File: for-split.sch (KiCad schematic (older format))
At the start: 77 parts, among them J1 TRRS, J2 TRRS, U1 ProMicro

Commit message: Increase size of switch cutouts
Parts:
- MX0:0, MX0:5: footprint idle-hands:MX_CUTOUT_VERT_PAD1 -> idle-hands:MX_CUTOUT_PAD1
- MX0:1, MX0:4: footprint idle-hands:MX_CUTOUT_VERT_PAD3 -> idle-hands:MX_CUTOUT_PAD3
- MX0:2, MX0:3, MX1:0, MX1:1, MX1:2, MX1:3, MX1:4, MX1:5, MX2:0, MX2:1, MX2:2, MX2:3, MX2:4, MX2:5, MX3:0, MX3:1, MX3:2, MX3:3, MX3:4, MX3:5, MX4:2, MX4:3: footprint idle-hands:MX_CUTOUT_VERT -> idle-hands:MX_CUTOUT
- MX4:1, MX4:4: footprint idle-hands:MX2U_CUTOUT_VERT -> idle-hands:MX2U_CUTOUT
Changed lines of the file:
@@
 Sheet 1 1
 Title "For Split - 6x4x2 key split keyboard"
-Date ""
-Rev ""
+Date "2018-03-18"
+Rev "2"
 Comp ""
 Comment1 ""
@@
 F 0 "MX1:0" H 5140 2590 50  0000 C CNN
 F 1 "MX1:11" H 4990 2400 50  0000 C CNN
-F 2 "idle-hands:MX_CUTOUT_VERT" H 4990 2480 60  0001 C CNN
+F 2 "idle-hands:MX_CUTOUT" H 4990 2480 60  0001 C CNN
 F 3 "" H 4990 2480 60  0000 C CNN
 	1    4990 2480
@@
 F 0 "MX1:1" H 6040 2590 50  0000 C CNN
 F 1 "MX1:10" H 5890 2400 50  0000 C CNN
-F 2 "idle-hands:MX_CUTOUT_VERT" H 5890 2480 60  0001 C CNN
+F 2 "idle-hands:MX_CUTOUT" H 5890 2480 60  0001 C CNN
 F 3 "" H 5890 2480 60  0000 C CNN
 	1    5890 2480
@@
 F 0 "MX1:2" H 6940 2590 50  0000 C CNN
 F 1 "MX1:9" H 6790 2400 50  0000 C CNN
-F 2 "idle-hands:MX_CUTOUT_VERT" H 6790 2480 60  0001 C CNN
+F 2 "idle-hands:MX_CUTOUT" H 6790 2480 60  0001 C CNN
 F 3 "" H 6790 2480 60  0000 C CNN
 	1    6790 2480
@@
 F 0 "MX1:3" H 7890 2590 50  0000 C CNN
 F 1 "MX1:8" H 7740 2400 50  0000 C CNN
-F 2 "idle-hands:MX_CUTOUT_VERT" H 7740 2480 60  0001 C CNN
+F 2 "idle-hands:MX_CUTOUT" H 7740 2480 60  0001 C CNN
 F 3 "" H 7740 2480 60  0000 C CNN
 	1    7740 2480
@@
 F 0 "MX1:4" H 8840 2590 50  0000 C CNN
 F 1 "MX1:7" H 8690 2400 50  0000 C CNN
-F 2 "idle-hands:MX_CUTOUT_VERT" H 8690 2480 60  0001 C CNN
+F 2 "idle-hands:MX_CUTOUT" H 8690 2480 60  0001 C CNN
 F 3 "" H 8690 2480 60  0000 C CNN
 	1    8690 2480
@@
 F 0 "MX0:0" H 5140 1840 50  0000 C CNN
 F 1 "MX0:11" H 4990 1650 50  0000 C CNN
-F 2 "idle-hands:MX_CUTOUT_VERT_PAD1" H 4990 1730 60  0001 C CNN
+F 2 "idle-hands:MX_CUTOUT_PAD1" H 4990 1730 60  0001 C CNN
 F 3 "" H 4990 1730 60  0000 C CNN
 	1    4990 1730
@@
 F 0 "MX0:1" H 6040 1840 50  0000 C CNN
 F 1 "MX0:10" H 5890 1650 50  0000 C CNN
-F 2 "idle-hands:MX_CUTOUT_VERT_PAD3" H 5890 1730 60  0001 C CNN
+F 2 "idle-hands:MX_CUTOUT_PAD3" H 5890 1730 60  0001 C CNN
 F 3 "" H 5890 1730 60  0000 C CNN
 	1    5890 1730
@@
 F 0 "MX0:2" H 6940 1840 50  0000 C CNN
 F 1 "MX0:9" H 6790 1650 50  0000 C CNN
-F 2 "idle-hands:MX_CUTOUT_VERT" H 6790 1730 60  0001 C CNN
+F 2 "idle-hands:MX_CUTOUT" H 6790 1730 60  0001 C CNN
 F 3 "" H 6790 1730 60  0000 C CNN
 	1    6790 1730
@@
 F 0 "MX0:3" H 7890 1840 50  0000 C CNN
 F 1 "MX0:8" H 7740 1650 50  0000 C CNN
-F 2 "idle-hands:MX_CUTOUT_VERT" H 7740 1730 60  0001 C CNN
+F 2 "idle-hands:MX_CUTOUT" H 7740 1730 60  0001 C CNN
 F 3 "" H 7740 1730 60  0000 C CNN
 	1    7740 1730
@@
 F 0 "MX0:4" H 8840 1840 50  0000 C CNN
 F 1 "MX0:7" H 8690 1650 50  0000 C CNN
-F 2 "idle-hands:MX_CUTOUT_VERT_PAD3" H 8690 1730 60  0001 C CNN
+F 2 "idle-hands:MX_CUTOUT_PAD3" H 8690 1730 60  0001 C CNN
 F 3 "" H 8690 1730 60  0000 C CNN
 	1    8690 1730
@@
 F 0 "MX2:0" H 5140 3340 50  0000 C CNN
 F 1 "MX2:11" H 4990 3150 50  0000 C CNN
-F 2 "idle-hands:MX_CUTOUT_VERT" H 4990 3230 60  0001 C CNN
+F 2 "idle-hands:MX_CUTOUT" H 4990 3230 60  0001 C CNN
 F 3 "" H 4990 3230 60  0000 C CNN
 	1    4990 3230
@@
 F 0 "MX2:1" H 6040 3340 50  0000 C CNN
 F 1 "MX2:10" H 5890 3150 50  0000 C CNN
-F 2 "idle-hands:MX_CUTOUT_VERT" H 5890 3230 60  0001 C CNN
+F 2 "idle-hands:MX_CUTOUT" H 5890 3230 60  0001 C CNN
 F 3 "" H 5890 3230 60  0000 C CNN
 	1    5890 3230
@@
 F 0 "MX2:2" H 6940 3340 50  0000 C CNN
 F 1 "MX2:9" H 6790 3150 50  0000 C CNN
-F 2 "idle-hands:MX_CUTOUT_VERT" H 6790 3230 60  0001 C CNN
+F 2 "idle-hands:MX_CUTOUT" H 6790 3230 60  0001 C CNN
 F 3 "" H 6790 3230 60  0000 C CNN
 	1    6790 3230
@@
 F 0 "MX2:3" H 7890 3340 50  0000 C CNN
 F 1 "MX2:8" H 7740 3150 50  0000 C CNN
-F 2 "idle-hands:MX_CUTOUT_VERT" H 7740 3230 60  0001 C CNN
+F 2 "idle-hands:MX_CUTOUT" H 7740 3230 60  0001 C CNN
 F 3 "" H 7740 3230 60  0000 C CNN
 	1    7740 3230
@@
 F 0 "MX2:4" H 8840 3340 50  0000 C CNN
 F 1 "MX2:7" H 8690 3150 50  0000 C CNN
-F 2 "idle-hands:MX_CUTOUT_VERT" H 8690 3230 60  0001 C CNN
+F 2 "idle-hands:MX_CUTOUT" H 8690 3230 60  0001 C CNN
 F 3 "" H 8690 3230 60  0000 C CNN
 	1    8690 3230
@@
 F 0 "MX3:1" H 6040 4090 50  0000 C CNN
 F 1 "MX3:10" H 5890 3900 50  0000 C CNN
-F 2 "idle-hands:MX_CUTOUT_VERT" H 5890 3980 60  0001 C CNN
+F 2 "idle-hands:MX_CUTOUT" H 5890 3980 60  0001 C CNN
 F 3 "" H 5890 3980 60  0000 C CNN
 	1    5890 3980
@@
 F 0 "MX3:2" H 6940 4090 50  0000 C CNN
 F 1 "MX3:9" H 6790 3900 50  0000 C CNN
-F 2 "idle-hands:MX_CUTOUT_VERT" H 6790 3980 60  0001 C CNN
+F 2 "idle-hands:MX_CUTOUT" H 6790 3980 60  0001 C CNN
 F 3 "" H 6790 3980 60  0000 C CNN
 	1    6790 3980
@@
 F 0 "MX3:3" H 7890 4090 50  0000 C CNN
 F 1 "MX3:8" H 7740 3900 50  0000 C CNN
-F 2 "idle-hands:MX_CUTOUT_VERT" H 7740 3980 60  0001 C CNN
+F 2 "idle-hands:MX_CUTOUT" H 7740 3980 60  0001 C CNN
 F 3 "" H 7740 3980 60  0000 C CNN
 	1    7740 3980
@@
 F 0 "MX3:4" H 8840 4090 50  0000 C CNN
 F 1 "MX3:7" H 8690 3900 50  0000 C CNN
-F 2 "idle-hands:MX_CUTOUT_VERT" H 8690 3980 60  0001 C CNN
+F 2 "idle-hands:MX_CUTOUT" H 8690 3980 60  0001 C CNN
 F 3 "" H 8690 3980 60  0000 C CNN
 	1    8690 3980
@@
 F 0 "MX3:0" H 5140 4090 50  0000 C CNN
 F 1 "MX3:11" H 4990 3900 50  0000 C CNN
-F 2 "idle-hands:MX_CUTOUT_VERT" H 4990 3980 60  0001 C CNN
+F 2 "idle-hands:MX_CUTOUT" H 4990 3980 60  0001 C CNN
 F 3 "" H 4990 3980 60  0000 C CNN
 	1    4990 3980
@@
 F 0 "MX1:5" H 9790 2590 50  0000 C CNN
 F 1 "MX1:6" H 9640 2400 50  0000 C CNN
-F 2 "idle-hands:MX_CUTOUT_VERT" H 9640 2480 60  0001 C CNN
+F 2 "idle-hands:MX_CUTOUT" H 9640 2480 60  0001 C CNN
 F 3 "" H 9640 2480 60  0000 C CNN
 	1    9640 2480
@@
 F 0 "MX0:5" H 9790 1840 50  0000 C CNN
 F 1 "MX0:6" H 9640 1650 50  0000 C CNN
-F 2 "idle-hands:MX_CUTOUT_VERT_PAD1" H 9640 1730 60  0001 C CNN
+F 2 "idle-hands:MX_CUTOUT_PAD1" H 9640 1730 60  0001 C CNN
 F 3 "" H 9640 1730 60  0000 C CNN
 	1    9640 1730
@@
 F 0 "MX2:5" H 9790 3340 50  0000 C CNN
 F 1 "MX2:6" H 9640 3150 50  0000 C CNN
-F 2 "idle-hands:MX_CUTOUT_VERT" H 9640 3230 60  0001 C CNN
+F 2 "idle-hands:MX_CUTOUT" H 9640 3230 60  0001 C CNN
 F 3 "" H 9640 3230 60  0000 C CNN
 	1    9640 3230
@@
 F 0 "MX3:5" H 9790 4090 50  0000 C CNN
 F 1 "MX3:6" H 9640 3900 50  0000 C CNN
-F 2 "idle-hands:MX_CUTOUT_VERT" H 9640 3980 60  0001 C CNN
+F 2 "idle-hands:MX_CUTOUT" H 9640 3980 60  0001 C CNN
 F 3 "" H 9640 3980 60  0000 C CNN
 	1    9640 3980
@@
 F 0 "MX4:1" H 6040 4820 50  0000 C CNN
 F 1 "MX4:10" H 5890 4630 50  0000 C CNN
-F 2 "idle-hands:MX2U_CUTOUT_VERT" H 5890 4710 60  0001 C CNN
+F 2 "idle-hands:MX2U_CUTOUT" H 5890 4710 60  0001 C CNN
 F 3 "" H 5890 4710 60  0000 C CNN
 	1    5890 4710
@@
 F 0 "MX4:2" H 6940 4820 50  0000 C CNN
 F 1 "MX4:9" H 6790 4630 50  0000 C CNN
-F 2 "idle-hands:MX_CUTOUT_VERT" H 6790 4710 60  0001 C CNN
+F 2 "idle-hands:MX_CUTOUT" H 6790 4710 60  0001 C CNN
 F 3 "" H 6790 4710 60  0000 C CNN
 	1    6790 4710
@@
 F 0 "MX4:3" H 7890 4820 50  0000 C CNN
 F 1 "MX4:8" H 7740 4630 50  0000 C CNN
-F 2 "idle-hands:MX_CUTOUT_VERT" H 7740 4710 60  0001 C CNN
+F 2 "idle-hands:MX_CUTOUT" H 7740 4710 60  0001 C CNN
 F 3 "" H 7740 4710 60  0000 C CNN
 	1    7740 4710
@@
 F 0 "MX4:4" H 8840 4820 50  0000 C CNN
 F 1 "MX4:7" H 8690 4630 50  0000 C CNN
-F 2 "idle-hands:MX2U_CUTOUT_VERT" H 8690 4710 60  0001 C CNN
+F 2 "idle-hands:MX2U_CUTOUT" H 8690 4710 60  0001 C CNN
 F 3 "" H 8690 4710 60  0000 C CNN
 	1    8690 4710

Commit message: Fix incorrect LED routing
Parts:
- MX0:4: footprint idle-hands:MX_CUTOUT_PAD3 -> idle-hands:MX_CUTOUT_PAD1
- MX0:5: footprint idle-hands:MX_CUTOUT_PAD1 -> idle-hands:MX_CUTOUT_PAD3
- MX4:4: footprint idle-hands:MX2U_CUTOUT -> idle-hands:MX
- MX4:5: footprint idle-hands:MX -> idle-hands:MX2U_CUTOUT
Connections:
- net GND: now also R1.1, R2.1
- net VCC: no longer R1.1, R2.1
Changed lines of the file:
@@
 LIBS:contrib
 LIBS:valves
-LIBS:for-idle-hands-cache
 LIBS:for-split-cache
 EELAYER 25 0
@@
 F 0 "MX0:4" H 8840 1840 50  0000 C CNN
 F 1 "MX0:7" H 8690 1650 50  0000 C CNN
-F 2 "idle-hands:MX_CUTOUT_PAD3" H 8690 1730 60  0001 C CNN
+F 2 "idle-hands:MX_CUTOUT_PAD1" H 8690 1730 60  0001 C CNN
 F 3 "" H 8690 1730 60  0000 C CNN
 	1    8690 1730
@@
 F 0 "MX0:5" H 9790 1840 50  0000 C CNN
 F 1 "MX0:6" H 9640 1650 50  0000 C CNN
-F 2 "idle-hands:MX_CUTOUT_PAD1" H 9640 1730 60  0001 C CNN
+F 2 "idle-hands:MX_CUTOUT_PAD3" H 9640 1730 60  0001 C CNN
 F 3 "" H 9640 1730 60  0000 C CNN
 	1    9640 1730
@@
 NoConn ~ 2630 3870
 NoConn ~ 1630 3470
-NoConn ~ 1630 3670
 NoConn ~ 1630 3570
 NoConn ~ 2630 3370
@@
 F 0 "MX4:4" H 8840 4820 50  0000 C CNN
 F 1 "MX4:7" H 8690 4630 50  0000 C CNN
-F 2 "idle-hands:MX2U_CUTOUT" H 8690 4710 60  0001 C CNN
+F 2 "idle-hands:MX" H 8690 4710 60  0001 C CNN
 F 3 "" H 8690 4710 60  0000 C CNN
 	1    8690 4710
@@
 F 0 "MX4:5" H 9790 4820 50  0000 C CNN
 F 1 "MX4:6" H 9640 4630 50  0000 C CNN
-F 2 "idle-hands:MX" H 9640 4710 60  0001 C CNN
+F 2 "idle-hands:MX2U_CUTOUT" H 9640 4710 60  0001 C CNN
 F 3 "" H 9640 4710 60  0000 C CNN
 	1    9640 4710
@@
 F 3 "" H 1770 5470 50  0001 C CNN
 	1    1770 5470
-	0    1    1    0
-$EndComp
-$Comp
-L VCC #PWR08
-U 1 1 5A9012EA
-P 1920 5470
-F 0 "#PWR08" H 1920 5320 50  0001 C CNN
-F 1 "VCC" H 1920 5620 50  0000 C CNN
-F 2 "" H 1920 5470 50  0001 C CNN
-F 3 "" H 1920 5470 50  0001 C CNN
-	1    1920 5470
 	0    1    1    0
 $EndComp
@@
 	0    1    1    0
 $EndComp
-$Comp
-L VCC #PWR09
-U 1 1 5A905603
-P 3420 5490
-F 0 "#PWR09" H 3420 5340 50  0001 C CNN
-F 1 "VCC" H 3420 5640 50  0000 C CNN
-F 2 "" H 3420 5490 50  0001 C CNN
-F 3 "" H 3420 5490 50  0001 C CNN
-	1    3420 5490
-	0    1    1    0
-$EndComp
 Text Label 2740 5490 2    60   ~ 0
 LED2
@@
 Connection ~ 3120 5660
 Connection ~ 2820 5660
+$Comp
+L GND #PWR08
+U 1 1 5AAEB9AB
+P 1920 5470
+F 0 "#PWR08" H 1920 5220 50  0001 C CNN
+F 1 "GND" H 1920 5320 50  0000 C CNN
+F 2 "" H 1920 5470 50  0001 C CNN
+F 3 "" H 1920 5470 50  0001 C CNN
+	1    1920 5470
+	0    -1   -1   0
+$EndComp
+$Comp
+L GND #PWR09
+U 1 1 5AAEBAA9
+P 3420 5490
+F 0 "#PWR09" H 3420 5240 50  0001 C CNN
+F 1 "GND" H 3420 5340 50  0000 C CNN
+F 2 "" H 3420 5490 50  0001 C CNN
+F 3 "" H 3420 5490 50  0001 C CNN
+	1    3420 5490
+	0    -1   -1   0
+$EndComp
+NoConn ~ 1630 3670
 $EndSCHEMATC

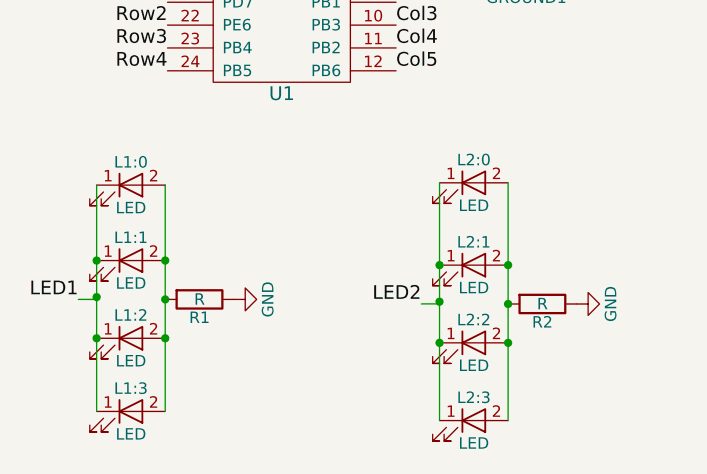
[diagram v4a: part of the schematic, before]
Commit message: Flip LED footprints to correct orientation
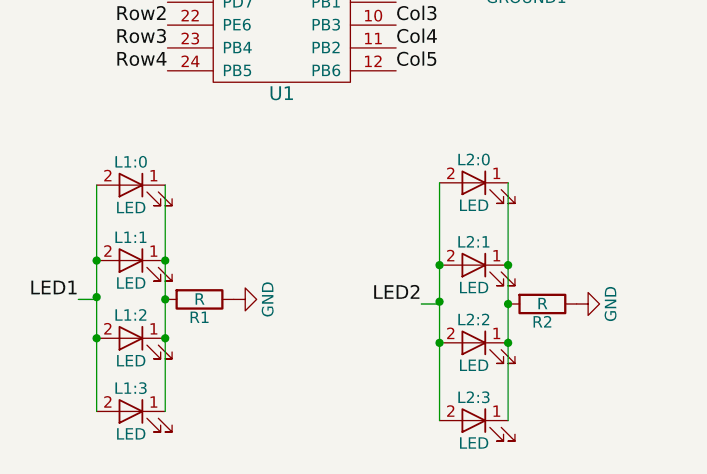
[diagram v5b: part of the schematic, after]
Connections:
- net LED1: now also L1:0.2 (A), L1:1.2 (A), L1:2.2 (A), L1:3.2 (A); no longer L1:0.1 (K), L1:1.1 (K), L1:2.1 (K), L1:3.1 (K)
- net LED2: now also L2:0.2 (A), L2:1.2 (A), L2:2.2 (A), L2:3.2 (A); no longer L2:0.1 (K), L2:1.1 (K), L2:2.1 (K), L2:3.1 (K)
- new net: L1:0.1 (K), L1:1.1 (K), L1:2.1 (K), L1:3.1 (K), R1.2
- new net: L2:0.1 (K), L2:1.1 (K), L2:2.1 (K), L2:3.1 (K), R2.2
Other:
- moved on the sheet: L1:0, L1:1, L1:2, L1:3, L2:0, L2:1, L2:2, L2:3
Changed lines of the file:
@@
 F 3 "" H 1470 4970 50  0001 C CNN
 	1    1470 4970
-	1    0    0    -1
+	-1   0    0    -1
 $EndComp
 $Comp
@@
 F 3 "" H 1470 5300 50  0001 C CNN
 	1    1470 5300
-	1    0    0    -1
+	-1   0    0    -1
 $EndComp
 Wire Wire Line
@@
 F 3 "" H 2970 4960 50  0001 C CNN
 	1    2970 4960
-	1    0    0    -1
+	-1   0    0    -1
 $EndComp
 $Comp
@@
 F 3 "" H 2970 5320 50  0001 C CNN
 	1    2970 5320
-	1    0    0    -1
+	-1   0    0    -1
 $EndComp
 Wire Wire Line
@@
 F 3 "" H 1470 5640 50  0001 C CNN
 	1    1470 5640
-	1    0    0    -1
+	-1   0    0    -1
 $EndComp
 $Comp
@@
 F 3 "" H 1470 5960 50  0001 C CNN
 	1    1470 5960
-	1    0    0    -1
+	-1   0    0    -1
 $EndComp
 Connection ~ 1320 5300
@@
 F 3 "" H 2970 5660 50  0001 C CNN
 	1    2970 5660
-	1    0    0    -1
+	-1   0    0    -1
 $EndComp
 $Comp
@@
 F 3 "" H 2970 6000 50  0001 C CNN
 	1    2970 6000
-	1    0    0    -1
+	-1   0    0    -1
 $EndComp
 Connection ~ 2820 5320

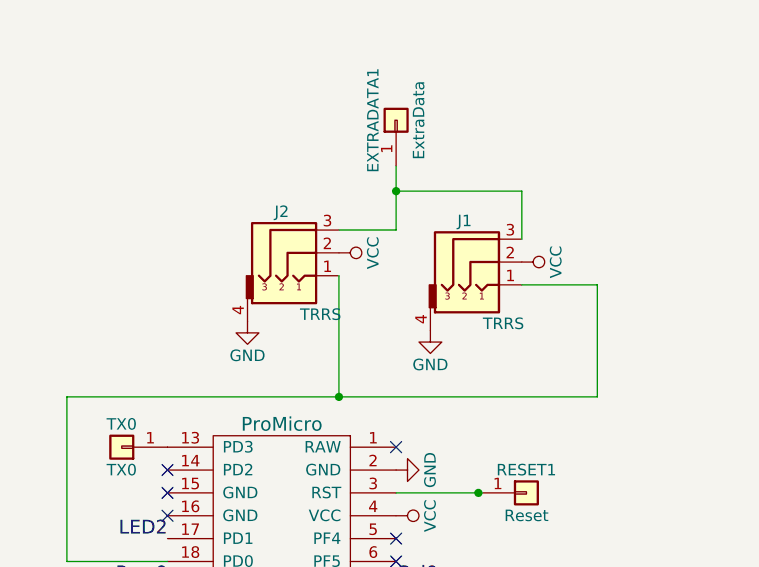
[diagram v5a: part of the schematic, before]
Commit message: Switch to through hole PJ320A socket
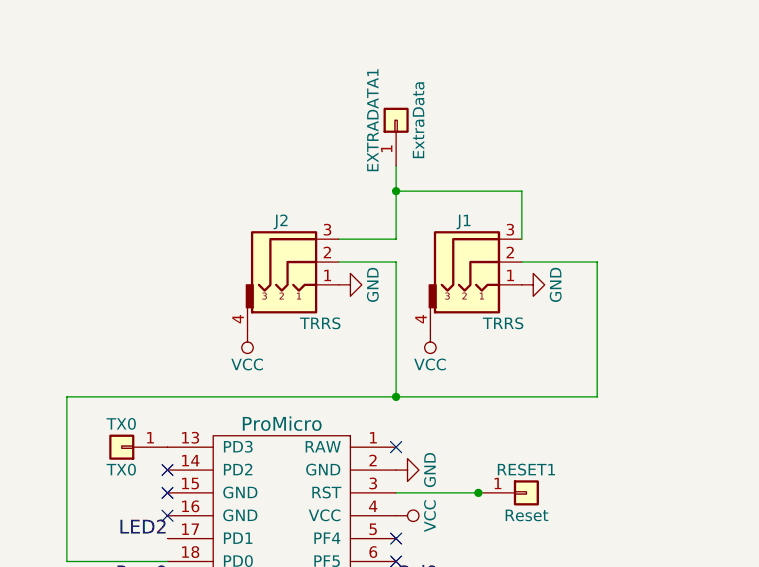
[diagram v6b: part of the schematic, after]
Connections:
- net GND: now also J1.1, J2.1; no longer J1.4, J2.4
- net VCC: now also J1.4, J2.4; no longer J1.2, J2.2
- new net: J1.2, J2.2, U1.18 (PD0)
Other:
- moved on the sheet: J2
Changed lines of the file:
@@
 L GND #PWR01
 U 1 1 59FA4C28
+P 3180 2660
+F 0 "#PWR01" H 3180 2410 50  0001 C CNN
+F 1 "GND" H 3180 2510 50  0000 C CNN
+F 2 "" H 3180 2660 50  0001 C CNN
+F 3 "" H 3180 2660 50  0001 C CNN
+	1    3180 2660
+	0    -1   -1   0
+$EndComp
+$Comp
+L VCC #PWR02
+U 1 1 59FA4D2C
 P 2780 2860
-F 0 "#PWR01" H 2780 2610 50  0001 C CNN
-F 1 "GND" H 2780 2710 50  0000 C CNN
+F 0 "#PWR02" H 2780 2710 50  0001 C CNN
+F 1 "VCC" H 2780 3010 50  0000 C CNN
 F 2 "" H 2780 2860 50  0001 C CNN
 F 3 "" H 2780 2860 50  0001 C CNN
 	1    2780 2860
-	1    0    0    -1
-$EndComp
-$Comp
-L VCC #PWR02
-U 1 1 59FA4D2C
-P 3180 2560
-F 0 "#PWR02" H 3180 2410 50  0001 C CNN
-F 1 "VCC" H 3180 2710 50  0000 C CNN
-F 2 "" H 3180 2560 50  0001 C CNN
-F 3 "" H 3180 2560 50  0001 C CNN
-	1    3180 2560
-	0    1    1    0
+	-1   0    0    1
 $EndComp
 $Comp
@@
 L Audio-Jack-4 J2
 U 1 1 5A73C569
-P 2180 2420
-F 0 "J2" H 2130 2500 50  0000 C CNN
-F 1 "TRRS" H 2300 2050 50  0000 C CNN
-F 2 "Connectors:PJ320D_3.5mm_Jack" H 2430 2520 50  0001 C CNN
-F 3 "" H 2430 2520 50  0001 C CNN
-	1    2180 2420
+P 2180 2460
+F 0 "J2" H 2130 2540 50  0000 C CNN
+F 1 "TRRS" H 2300 2090 50  0000 C CNN
+F 2 "Connectors:PJ320D_3.5mm_Jack" H 2430 2560 50  0001 C CNN
+F 3 "" H 2430 2560 50  0001 C CNN
+	1    2180 2460
 	1    0    0    -1
 $EndComp
@@
 L GND #PWR06
 U 1 1 5A73C765
-P 1980 2820
-F 0 "#PWR06" H 1980 2570 50  0001 C CNN
-F 1 "GND" H 1980 2670 50  0000 C CNN
-F 2 "" H 1980 2820 50  0001 C CNN
-F 3 "" H 1980 2820 50  0001 C CNN
-	1    1980 2820
-	1    0    0    -1
+P 2380 2660
+F 0 "#PWR06" H 2380 2410 50  0001 C CNN
+F 1 "GND" H 2380 2510 50  0000 C CNN
+F 2 "" H 2380 2660 50  0001 C CNN
+F 3 "" H 2380 2660 50  0001 C CNN
+	1    2380 2660
+	0    -1   -1   0
 $EndComp
 $Comp
 L VCC #PWR07
 U 1 1 5A73C889
-P 2380 2520
-F 0 "#PWR07" H 2380 2370 50  0001 C CNN
-F 1 "VCC" H 2380 2670 50  0000 C CNN
-F 2 "" H 2380 2520 50  0001 C CNN
-F 3 "" H 2380 2520 50  0001 C CNN
-	1    2380 2520
-	0    1    1    0
+P 1980 2860
+F 0 "#PWR07" H 1980 2710 50  0001 C CNN
+F 1 "VCC" H 1980 3010 50  0000 C CNN
+F 2 "" H 1980 2860 50  0001 C CNN
+F 3 "" H 1980 2860 50  0001 C CNN
+	1    1980 2860
+	-1   0    0    1
 $EndComp
 $Comp
@@
 $EndComp
 Wire Wire Line
-	3510 2660 3180 2660
-Wire Wire Line
-	3510 3150 3510 2660
+	3510 3150 3510 2560
 Connection ~ 5290 3630
 Connection ~ 5290 2880
@@
 	2630 3570 3000 3570
 Wire Wire Line
-	3510 3150 1190 3150
+	1190 3150 3510 3150
 Wire Wire Line
 	1190 3870 1630 3870
@@
 Wire Wire Line
 	1190 3150 1190 3870
-Wire Wire Line
-	2380 2620 2380 3150
-Connection ~ 2380 3150
 Connection ~ 6190 5110
 Connection ~ 8040 5110
@@
 Connection ~ 4690 3980
 Wire Wire Line
-	2380 2420 2630 2420
-Wire Wire Line
-	2630 2420 2630 2140
+	2630 2460 2380 2460
+Wire Wire Line
+	2630 2140 2630 2460
 Wire Wire Line
 	3180 2460 3180 2250
@@
 $EndComp
 NoConn ~ 1630 3670
+Wire Wire Line
+	3510 2560 3180 2560
+Wire Wire Line
+	2380 2560 2630 2560
+Wire Wire Line
+	2630 2560 2630 3150
+Connection ~ 2630 3150
 $EndSCHEMATC
